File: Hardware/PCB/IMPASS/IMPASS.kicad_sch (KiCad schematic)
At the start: 0 parts

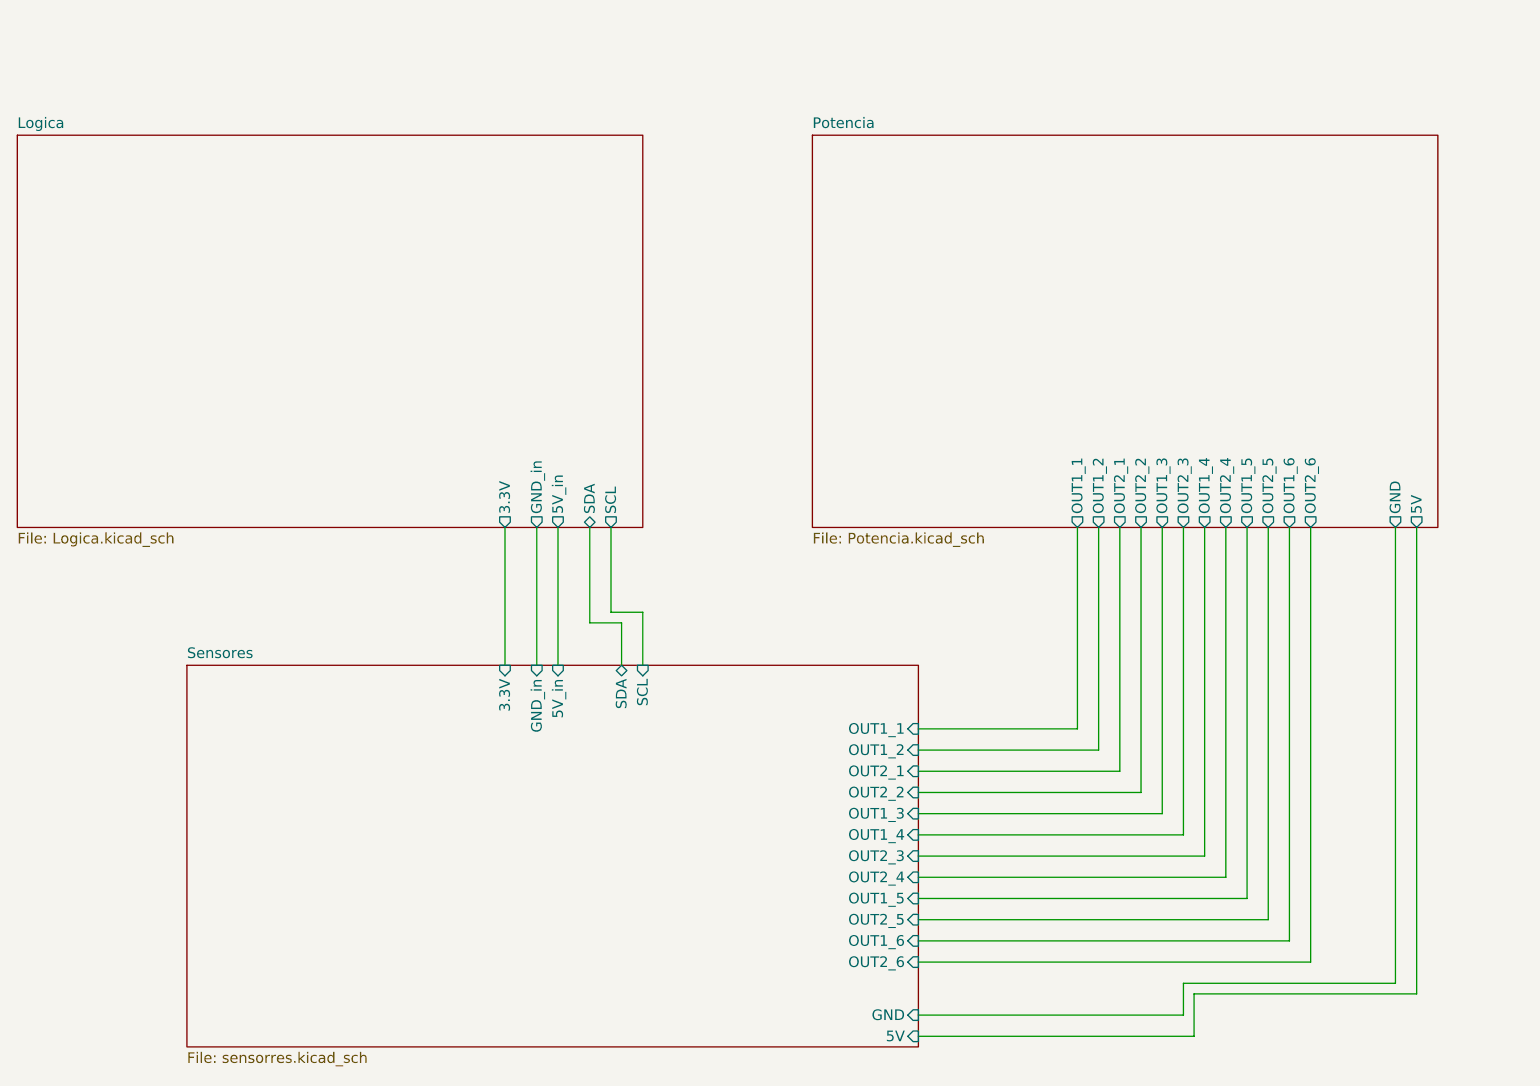
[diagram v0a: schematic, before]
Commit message: Restore all the schematics
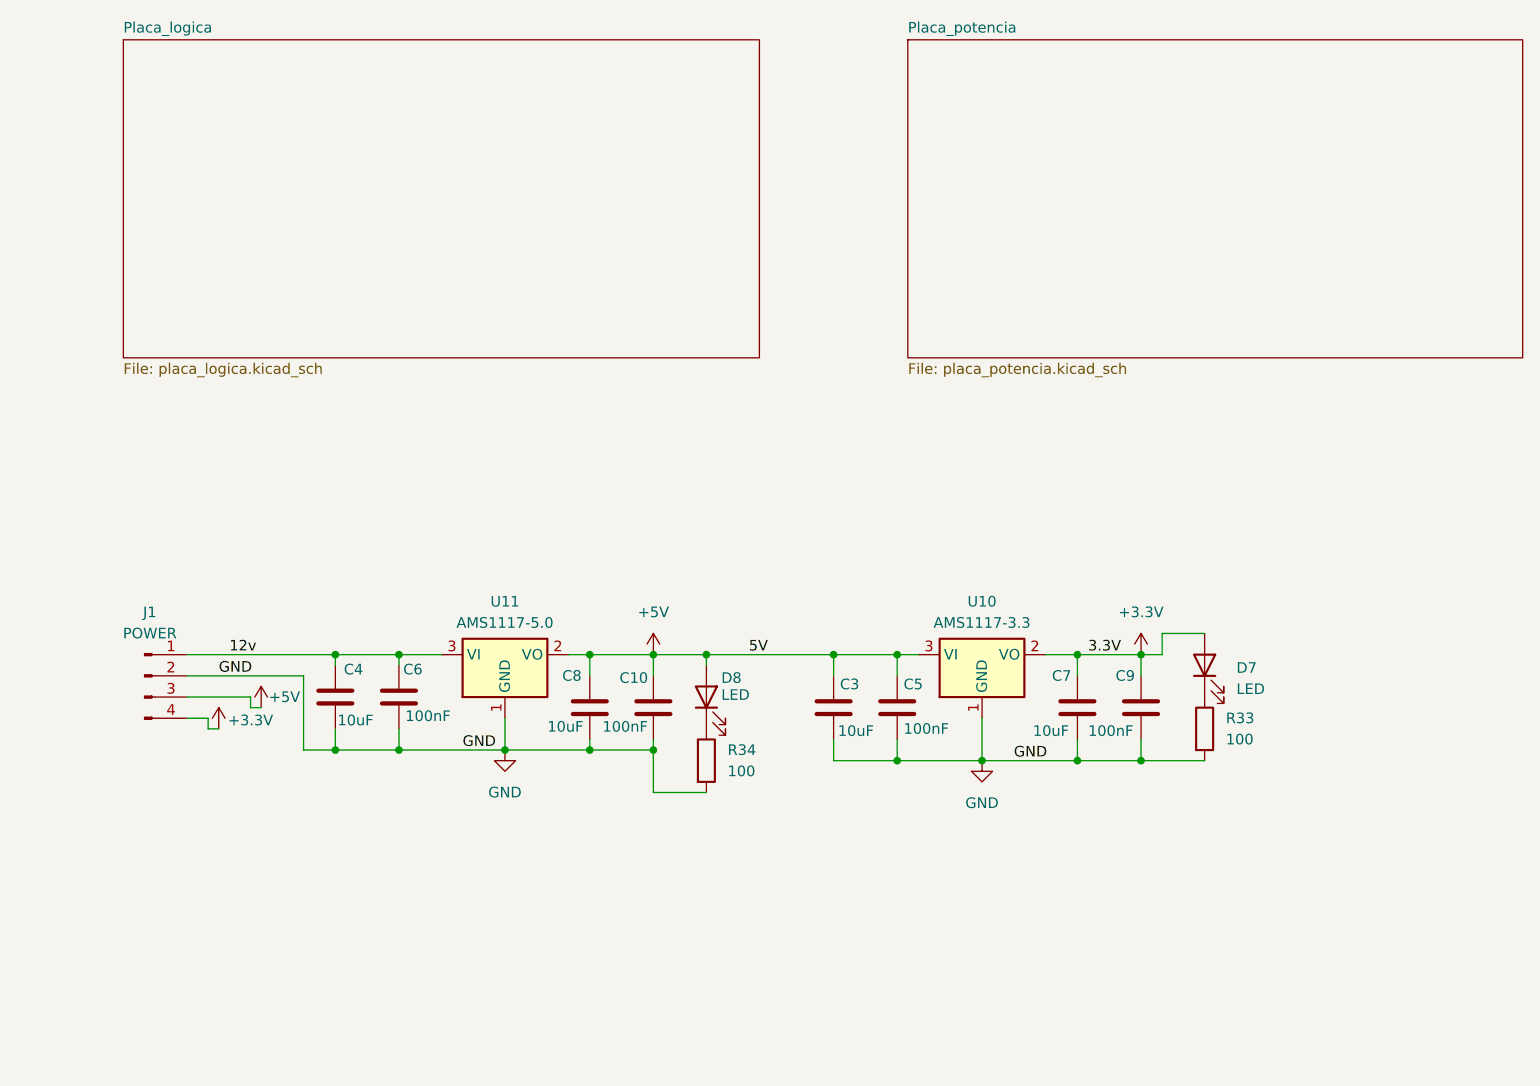
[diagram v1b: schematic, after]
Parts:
- added C10, C5, C6, C9: 100nF, Capacitor_SMD:C_0603_1608Metric, symbol Device:C
- added C3, C4, C7, C8: 10uF, Capacitor_SMD:C_0805_2012Metric, symbol Device:C
- added D7, D8: LED, LED_SMD:LED_0603_1608Metric, symbol Device:LED
- added J1: POWER, Connector_PinHeader_2.54mm:PinHeader_1x04_P2.54mm_Vertical, symbol Connector:Conn_01x04_Pin
- added R33, R34: 100, Resistor_SMD:R_0603_1608Metric, symbol Device:R
- added U10: AMS1117-3.3, Package_TO_SOT_SMD:SOT-223-3_TabPin2, symbol Regulator_Linear:AMS1117-3.3
- added U11: AMS1117-5.0, Package_TO_SOT_SMD:SOT-223-3_TabPin2, symbol Regulator_Linear:AMS1117-5.0
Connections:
- new net: D7.1 (K), R33.1
- new net: D8.1 (K), R34.1
- new net +3.3V: C7.1, C9.1, D7.2 (A), J1.4 (Pin_4), U10.2 (VO)
- new net +5V: C10.1, C3.1, C5.1, C8.1, D8.2 (A), J1.3 (Pin_3), U10.3 (VI), U11.2 (VO)
- new net 12v: C4.1, C6.1, J1.1 (Pin_1), U11.3 (VI)
- new net GND: C10.2, C3.2, C4.2, C5.2, C6.2, C7.2, C8.2, C9.2, J1.2 (Pin_2), R33.2, R34.2, U10.1 (GND), U11.1 (GND)
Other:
- removed sheet Logica
- removed sheet Potencia
- removed sheet Sensores
- added sheet Placa_logica (placa_logica.kicad_sch)
- added sheet Placa_potencia (placa_potencia.kicad_sch)
- company: (none) -> Luis Miguel Carmona Cortés
- title: (none) -> IMPASS 

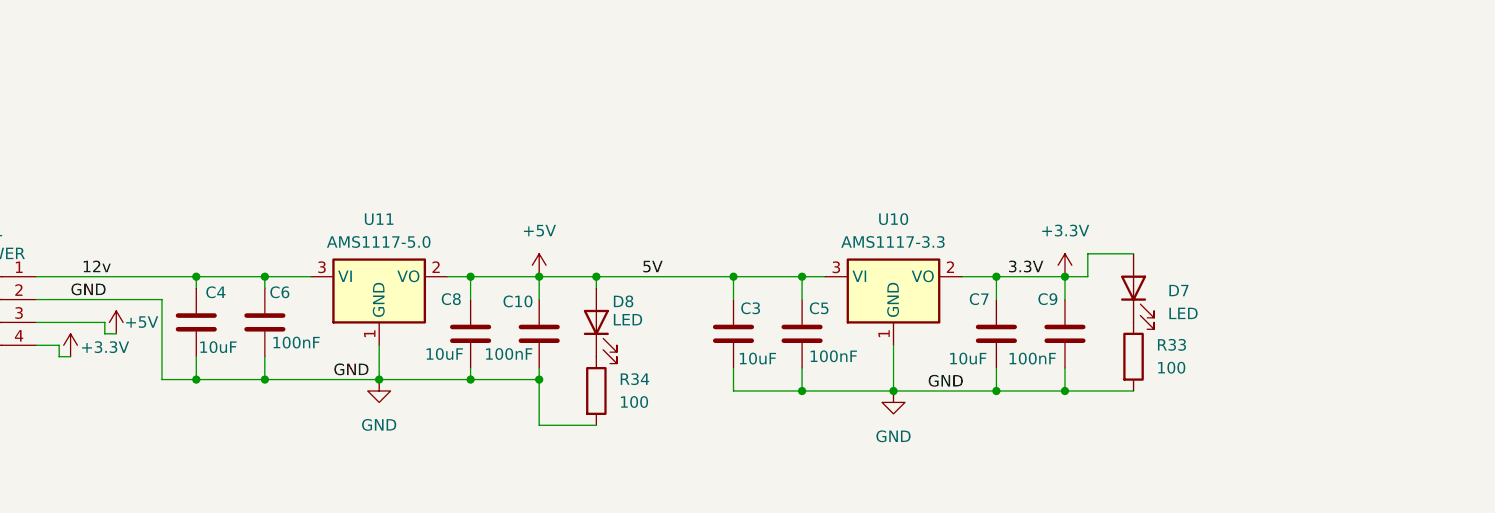
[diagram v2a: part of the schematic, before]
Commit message: Hardware: update schematic and PCB layout 	- Replace the LDOs with buck converters 	- Replace AD5047D with LIS3DH
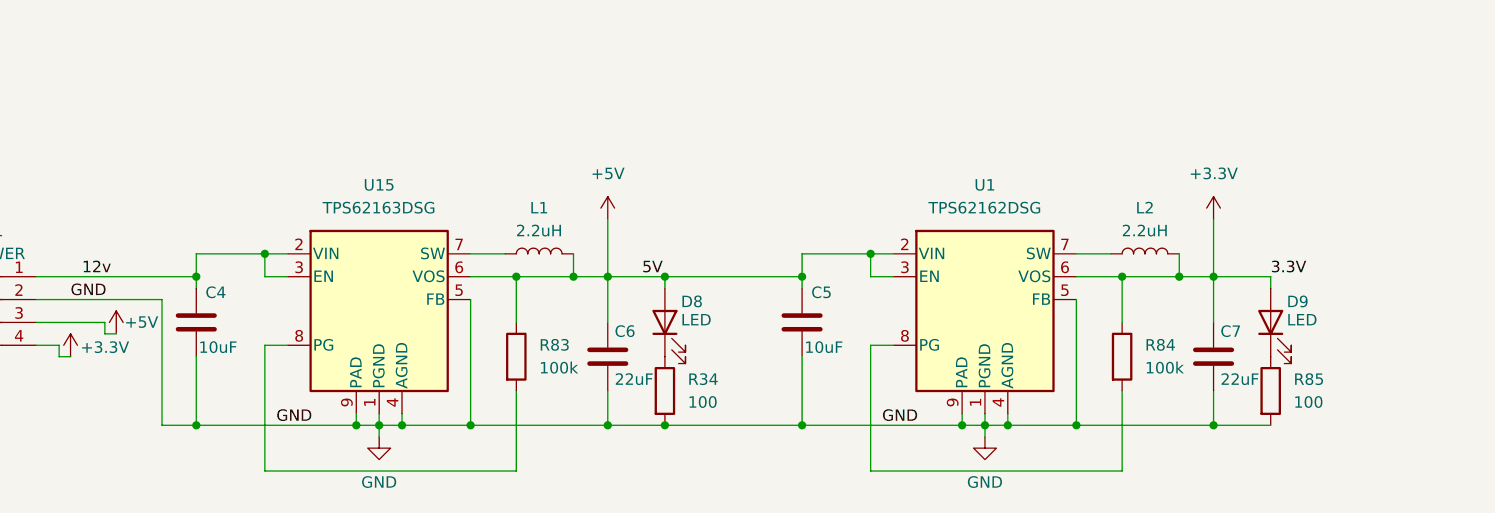
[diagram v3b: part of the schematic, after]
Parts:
- removed C10, C9: 100nF, Capacitor_SMD:C_0603_1608Metric, symbol Device:C
- removed C3, C8: 10uF, Capacitor_SMD:C_0805_2012Metric, symbol Device:C
- removed D7: LED, LED_SMD:LED_0603_1608Metric, symbol Device:LED
- removed R33: 100, Resistor_SMD:R_0603_1608Metric, symbol Device:R
- removed U10: AMS1117-3.3, Package_TO_SOT_SMD:SOT-223-3_TabPin2, symbol Regulator_Linear:AMS1117-3.3
- removed U11: AMS1117-5.0, Package_TO_SOT_SMD:SOT-223-3_TabPin2, symbol Regulator_Linear:AMS1117-5.0
- added D9: LED, LED_SMD:LED_0603_1608Metric, symbol Device:LED
- added L1, L2: 2.2uH, Inductor_SMD:L_0603_1608Metric, symbol Device:L
- added R83, R84: 100k, Resistor_SMD:R_0603_1608Metric, symbol Device:R
- added R85: 100, Resistor_SMD:R_0603_1608Metric, symbol Device:R
- added U1: TPS62162DSG, Package_SON:WSON-8-1EP_2x2mm_P0.5mm_EP0.9x1.6mm_ThermalVias, symbol Regulator_Switching:TPS62162DSG
- added U15: TPS62163DSG, Package_SON:WSON-8-1EP_2x2mm_P0.5mm_EP0.9x1.6mm_ThermalVias, symbol Regulator_Switching:TPS62163DSG
- C5: value 100nF -> 10uF; footprint Capacitor_SMD:C_0603_1608Metric -> Capacitor_SMD:C_0805_2012Metric
- C6: value 100nF -> 22uF
- C7: value 10uF -> 22uF; footprint Capacitor_SMD:C_0805_2012Metric -> Capacitor_SMD:C_0603_1608Metric
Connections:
- net +3.3V: now also D9.2 (A), L2.2, R84.1, U1.6 (VOS)
- net +5V: now also C6.1, L1.2, R83.1, U1.2 (VIN), U1.3 (EN), U15.6 (VOS)
- net 12v: now also U15.2 (VIN), U15.3 (EN); no longer C6.1
- net GND: now also R85.2, U1.1 (PGND), U1.4 (AGND), U1.5 (FB), U1.9 (PAD), U15.1 (PGND), U15.4 (AGND), U15.5 (FB), U15.9 (PAD)
- new net: R83.2, U15.8 (PG)
- new net: D9.1 (K), R85.1
- new net: L2.1, U1.7 (SW)
- new net: R84.2, U1.8 (PG)
- new net: L1.1, U15.7 (SW)
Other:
- moved on the sheet: D8, R34
